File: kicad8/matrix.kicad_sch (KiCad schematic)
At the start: 183 parts, among them SW1 ROT_SKYLOONG_HS

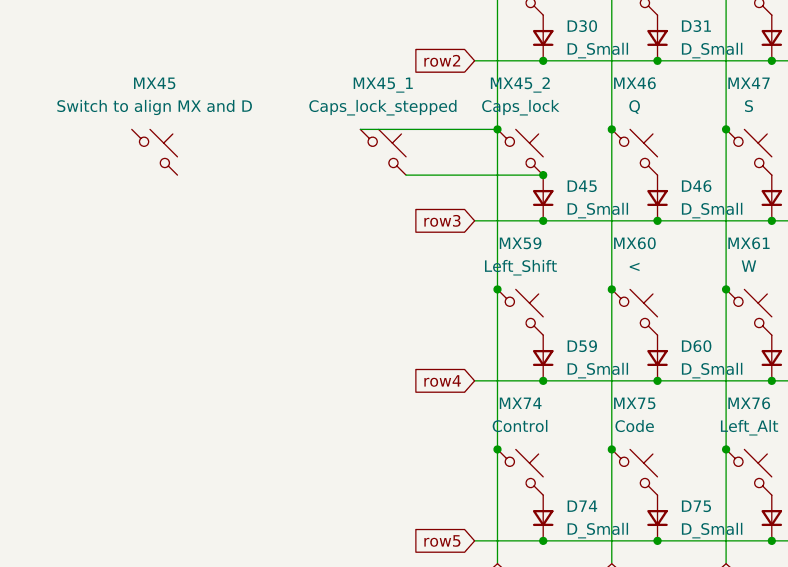
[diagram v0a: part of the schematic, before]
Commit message: Removed: old RGB file
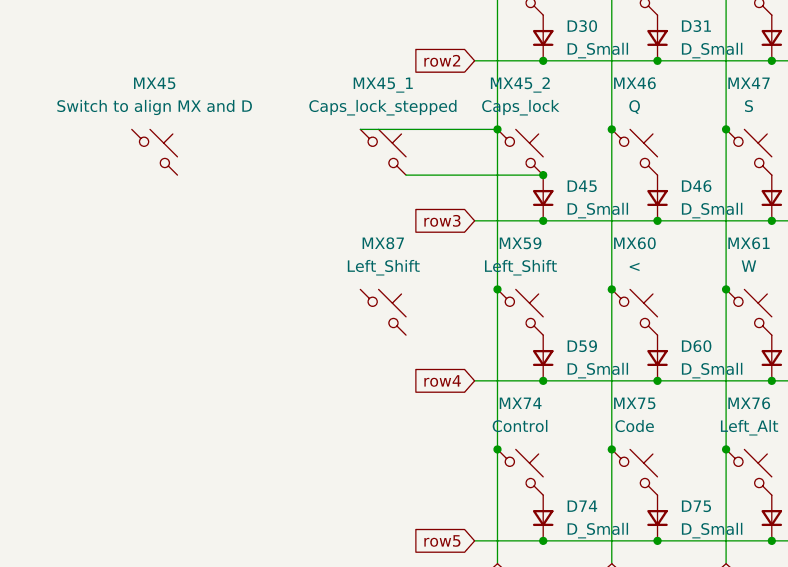
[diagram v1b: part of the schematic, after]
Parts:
- added MX87: Left_Shift, PCM_marbastlib-mx:SW_MX_HS_CPG151101S11_1u, symbol PCM_marbastlib-mx:MX_SW_HS_CPG151101S11
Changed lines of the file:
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@@
+	)
+	(symbol
+		(lib_id "PCM_marbastlib-mx:MX_SW_HS_CPG151101S11")
+		(at 49.53 96.52 0)
+		(unit 1)
+		(exclude_from_sim no)
+		(in_bom yes)
+		(on_board yes)
+		(dnp no)
+		(fields_autoplaced yes)
+		(property "Reference" "MX87"
+			(at 49.53 88.9 0)
+			(effects
+				(font
+					(size 1.27 1.27)
+				)
+			)
+		)
+		(property "Value" "Left_Shift"
+			(at 49.53 91.44 0)
+			(effects
+				(font
+					(size 1.27 1.27)
+				)
+			)
+		)
+		(property "Footprint" "PCM_marbastlib-mx:SW_MX_HS_CPG151101S11_1u"
+			(at 49.53 96.52 0)
+			(effects
+				(font
+					(size 1.27 1.27)
+				)
+				(hide yes)
+			)
+		)
+		(property "Datasheet" "~"
+			(at 49.53 96.52 0)
+			(effects
+				(font
+					(size 1.27 1.27)
+				)
+				(hide yes)
+			)
+		)
+		(property "Description" "Push button switch, normally open, two pins, 45° tilted, Kailh CPG151101S11 for Cherry MX style switches"
+			(at 49.53 96.52 0)
+			(effects
+				(font
+					(size 1.27 1.27)
+				)
+				(hide yes)
+			)
+		)
+		(pin "1"
+		)
+		(pin "2"
+		)
+		(instances
+			(project "kicad8"
+				(path "/4d291fcf-fdf2-46ba-aa57-60bc75f9cc32/2b97a220-2f1a-429f-8815-0fa3b3b8491d"
+					(reference "MX87")
+					(unit 1)
+				)
+			)
+		)
 	)
 	(symbol

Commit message: Initial branch commit
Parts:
- removed MX87: Left_Shift, PCM_marbastlib-mx:SW_MX_HS_CPG151101S11_1u, symbol PCM_marbastlib-mx:MX_SW_HS_CPG151101S11
- R5: footprint Diode_SMD:D_SOD-123 -> Resistor_SMD:R_0402_1005Metric
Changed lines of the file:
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@@
 	)
 	(symbol
-		(lib_id "PCM_marbastlib-mx:MX_SW_HS_CPG151101S11")
-		(at 49.53 96.52 0)
-		(unit 1)
-		(exclude_from_sim no)
-		(in_bom yes)
-		(on_board yes)
-		(dnp no)
-		(fields_autoplaced yes)
-		(property "Reference" "MX87"
-			(at 49.53 88.9 0)
-			(effects
-				(font
-					(size 1.27 1.27)
-				)
-			)
-		)
-		(property "Value" "Left_Shift"
-			(at 49.53 91.44 0)
-			(effects
-				(font
-					(size 1.27 1.27)
-				)
-			)
-		)
-		(property "Footprint" "PCM_marbastlib-mx:SW_MX_HS_CPG151101S11_1u"
-			(at 49.53 96.52 0)
-			(effects
-				(font
-					(size 1.27 1.27)
-				)
-				(hide yes)
-			)
-		)
-		(property "Datasheet" "~"
-			(at 49.53 96.52 0)
-			(effects
-				(font
-					(size 1.27 1.27)
-				)
-				(hide yes)
-			)
-		)
-		(property "Description" "Push button switch, normally open, two pins, 45° tilted, Kailh CPG151101S11 for Cherry MX style switches"
-			(at 49.53 96.52 0)
-			(effects
-				(font
-					(size 1.27 1.27)
-				)
-				(hide yes)
-			)
-		)
-		(pin "1"
-		)
-		(pin "2"
-		)
-		(instances
-			(project "kicad8"
-				(path "/4d291fcf-fdf2-46ba-aa57-60bc75f9cc32/2b97a220-2f1a-429f-8815-0fa3b3b8491d"
-					(reference "MX87")
-					(unit 1)
-				)
-			)
-		)
-	)
-	(symbol
 		(lib_id "Device:D_Small")
 		(at 194.31 66.04 90)
@@
 			)
 		)
-		(property "Footprint" "Diode_SMD:D_SOD-123"
+		(property "Footprint" "Resistor_SMD:R_0402_1005Metric"
 			(at 83.82 151.13 0)
 			(effects
